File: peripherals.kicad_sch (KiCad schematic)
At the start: 50 parts, among them J5 Out_to_display, U1 Boost Converter - TPS61169DCKR, U3 RA8875L3N, U7 74HC4050D, Y1 20MHz

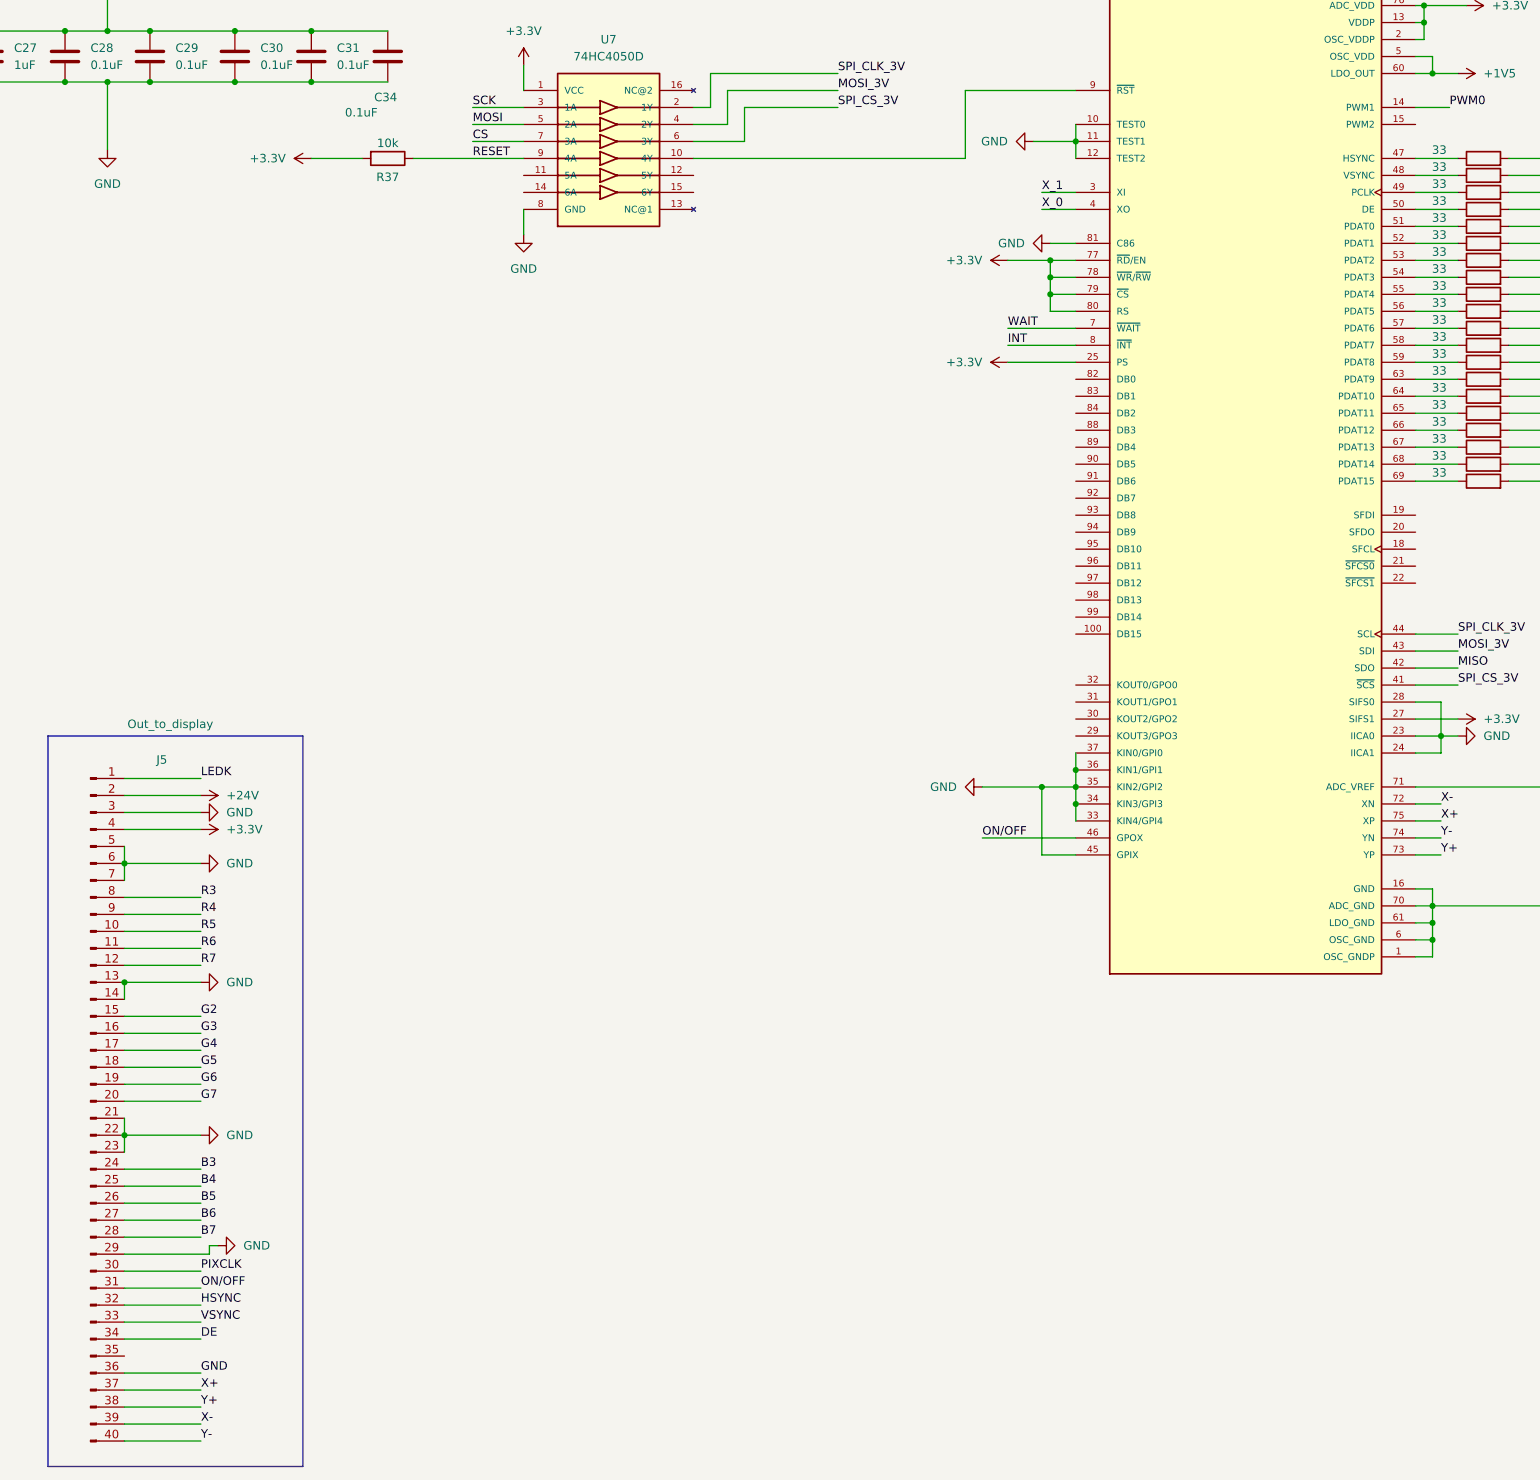
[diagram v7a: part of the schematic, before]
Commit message: added 10 pin stlink and fixed a bunch of errors and warnings
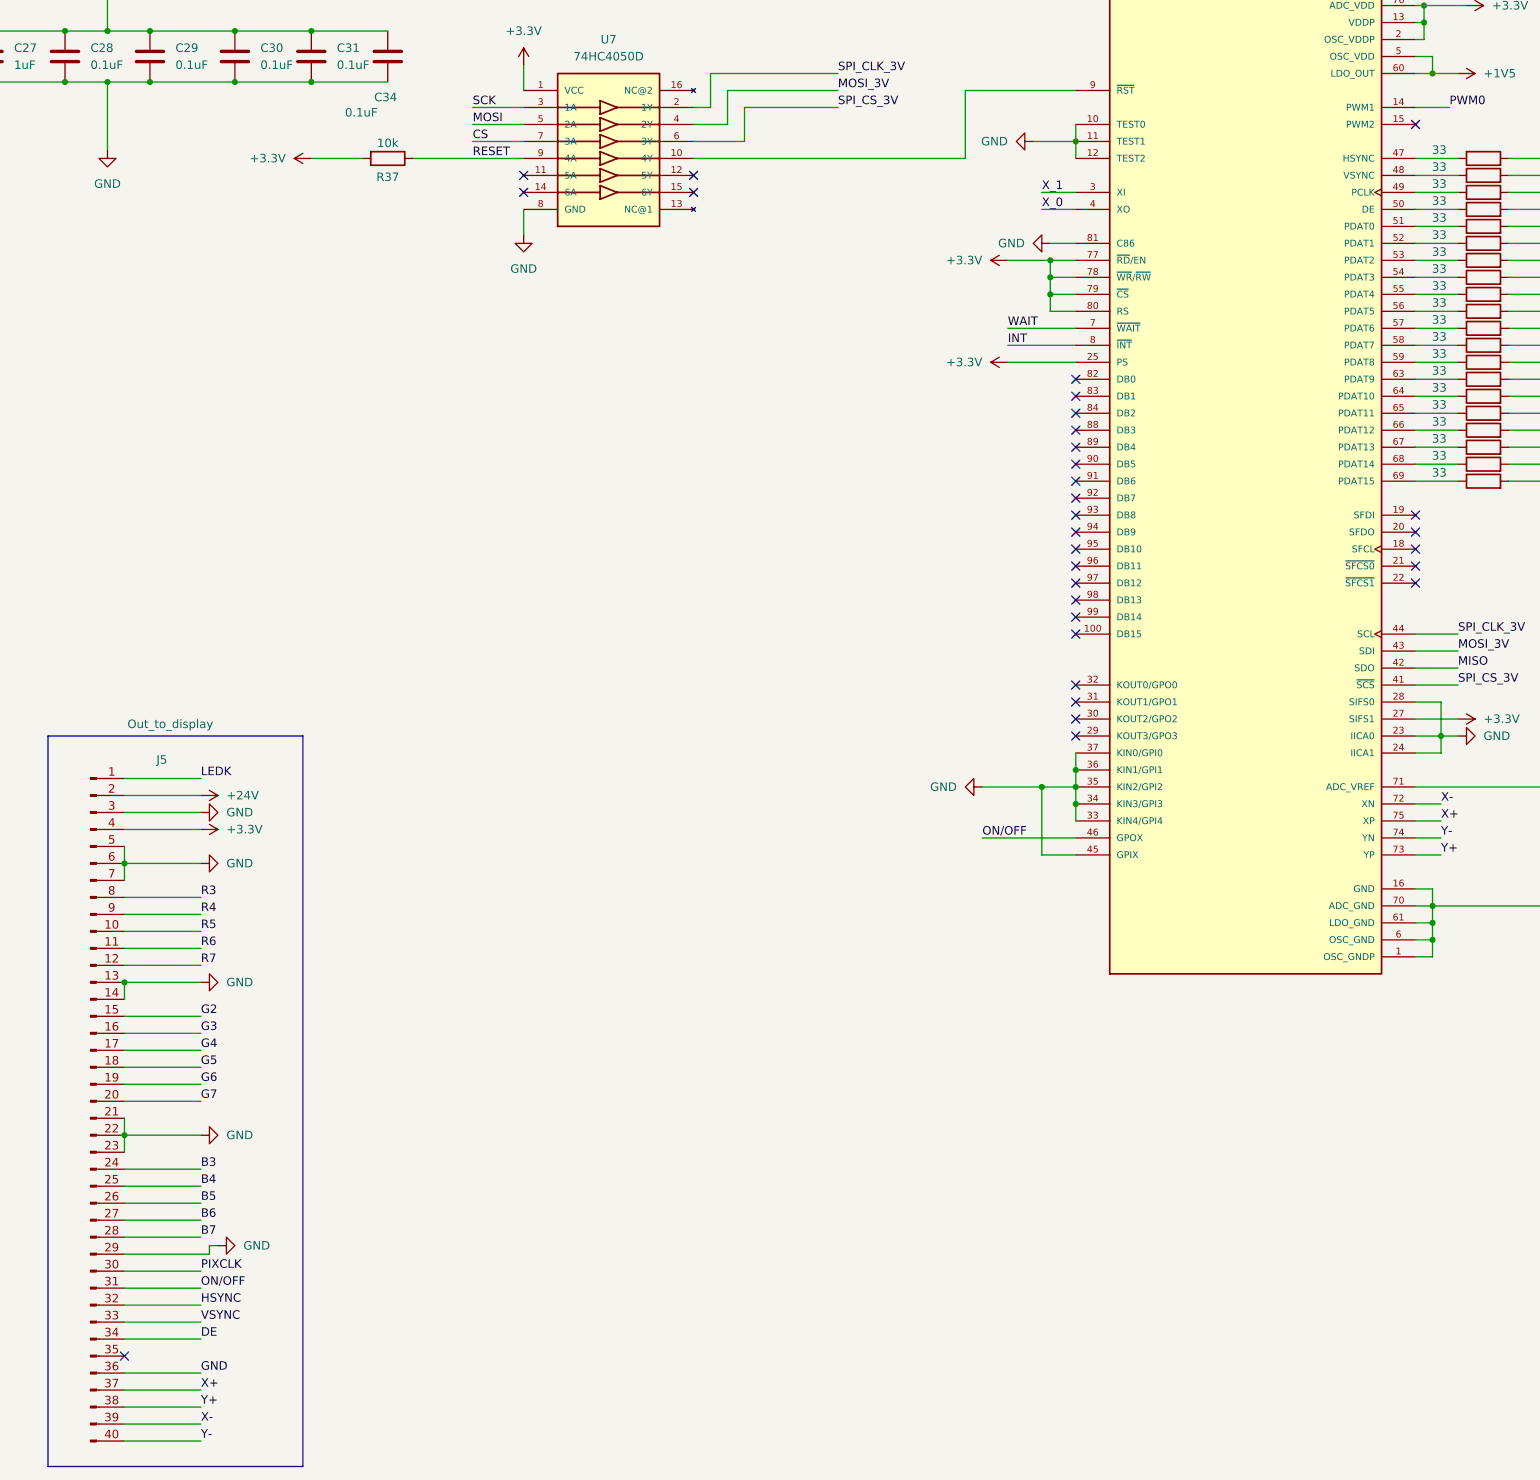
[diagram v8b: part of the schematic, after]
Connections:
- no-connect marks 0 -> 31
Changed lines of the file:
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@@
 		(color 0 0 0 0)
+	)
+	(no_connect
+		(at 421.64 119.38)
+	)
+	(no_connect
+		(at 421.64 137.16)
+	)
+	(no_connect
+		(at 421.64 104.14)
+	)
+	(no_connect
+		(at 364.49 68.58)
+	)
+	(no_connect
+		(at 421.64 149.86)
+	)
+	(no_connect
+		(at 421.64 144.78)
+	)
+	(no_connect
+		(at 421.64 101.6)
+	)
+	(no_connect
+		(at 472.44 127)
+	)
+	(no_connect
+		(at 364.49 71.12)
+	)
+	(no_connect
+		(at 421.64 134.62)
+	)
+	(no_connect
+		(at 472.44 60.96)
+	)
+	(no_connect
+		(at 421.64 99.06)
+	)
+	(no_connect
+		(at 421.64 116.84)
+	)
+	(no_connect
+		(at 472.44 129.54)
+	)
+	(no_connect
+		(at 421.64 147.32)
+	)
+	(no_connect
+		(at 472.44 124.46)
+	)
+	(no_connect
+		(at 421.64 129.54)
+	)
+	(no_connect
+		(at 472.44 119.38)
+	)
+	(no_connect
+		(at 421.64 127)
+	)
+	(no_connect
+		(at 421.64 124.46)
+	)
+	(no_connect
+		(at 421.64 132.08)
+	)
+	(no_connect
+		(at 339.09 71.12)
+	)
+	(no_connect
+		(at 421.64 114.3)
+	)
+	(no_connect
+		(at 339.09 68.58)
+	)
+	(no_connect
+		(at 421.64 111.76)
+	)
+	(no_connect
+		(at 421.64 106.68)
+	)
+	(no_connect
+		(at 421.64 152.4)
+	)
+	(no_connect
+		(at 279.4 245.11)
+	)
+	(no_connect
+		(at 421.64 121.92)
+	)
+	(no_connect
+		(at 421.64 109.22)
+	)
+	(no_connect
+		(at 472.44 121.92)
 	)
 	(wire
